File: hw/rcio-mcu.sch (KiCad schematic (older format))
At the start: 26 parts

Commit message: hw: Use PB9 (TIM17 CH1) for FAN RPM input
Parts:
- removed XP?: FAN, symbol Connector_Generic:Conn_01x02
- added XP?: FAN, symbol Connector_Generic:Conn_01x03
- R?: value 10k -> 4.7k
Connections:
- net labels added: FAN_RPM
- no-connect marks 15 -> 14
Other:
- moved on the sheet: DD?, R?, XP?

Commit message: hw: replace STM console and SWD with one connector. Rpi I2C and UART to DroneCode GPS port
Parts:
- removed XP?: SWD, symbol dronecode-conn:stm_swdo
- removed XP?: DBG UART, symbol Connector_Generic:Conn_01x03
- added R?: 47k, symbol Device:R
- added XP?: DC-Debug, symbol dronecode-conn:DC-Debug
- R?: value 4.7k -> 10k
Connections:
- net labels removed: BOOT0, ~NRST
- no-connect marks 14 -> 13
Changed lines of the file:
@@
 $EndDescr
-$Comp
-L dronecode-conn:stm_swdo XP?
-U 1 1 5AC130B8
-P 13250 8100
-F 0 "XP?" H 13478 8153 60  0000 L CNN
-F 1 "SWD" H 13478 8047 60  0000 L CNN
-F 2 "" H 13250 8100 60  0001 C CNN
-F 3 "" H 13250 8100 60  0001 C CNN
-	1    13250 8100
-	1    0    0    -1
-$EndComp
 $Comp
 L MCU_ST_STM32:STM32F030CCTx DD?
@@
 Wire Wire Line
 	3750 2050 4800 2050
-Text Label 4000 2050 0    60   ~ 0
-~NRST
 $Comp
 L power:+3.3V #PWR?
 U 1 1 5AC3643C
-P 12700 7700
-F 0 "#PWR?" H 12700 7550 50  0001 C CNN
-F 1 "+3.3V" H 12715 7873 50  0000 C CNN
-F 2 "" H 12700 7700 50  0001 C CNN
-F 3 "" H 12700 7700 50  0001 C CNN
-	1    12700 7700
+P 11900 7950
+F 0 "#PWR?" H 11900 7800 50  0001 C CNN
+F 1 "+3.3V" H 11915 8123 50  0000 C CNN
+F 2 "" H 11900 7950 50  0001 C CNN
+F 3 "" H 11900 7950 50  0001 C CNN
+	1    11900 7950
 	1    0    0    -1
 $EndComp
@@
 $EndComp
 Wire Wire Line
-	12850 7850 12700 7850
-Wire Wire Line
-	12700 7850 12700 7700
-Wire Wire Line
-	12850 8050 12700 8050
-Wire Wire Line
-	12700 8050 12700 8500
-Wire Wire Line
-	12850 7950 12300 7950
-Wire Wire Line
-	12850 8150 12300 8150
-Wire Wire Line
-	12850 8250 12300 8250
-Text Label 12300 7950 0    60   ~ 0
+	12050 8500 11500 8500
+Wire Wire Line
+	12050 8400 11500 8400
+Text Label 11500 8500 0    60   ~ 0
 SWCLK
-Text Label 12300 8150 0    60   ~ 0
+Text Label 11500 8400 0    60   ~ 0
 SWDIO
-Text Label 12300 8250 0    60   ~ 0
-~NRST
 Text GLabel 11300 3850 2    60   Input ~ 0
 RPI_SPI0_MOSI
@@
 Text GLabel 11300 4250 2    60   Output ~ 0
 SERVO3
-Text GLabel 13050 2600 0    60   UnSpc ~ 0
+Text GLabel 13050 2200 0    60   UnSpc ~ 0
 ADC_Vbat
-Text GLabel 13050 2450 0    60   UnSpc ~ 0
+Text GLabel 13850 2600 2    60   UnSpc ~ 0
 ADC_V5hat
 $Comp
@@
 Wire Wire Line
 	13600 3650 13600 3750
-Wire Wire Line
-	13050 2600 13200 2600
 $Comp
 L power:GND #PWR?
@@
 P 13200 3500
 F 0 "R?" H 13270 3546 50  0000 L CNN
-F 1 "4.7k" H 13270 3455 50  0000 L CNN
+F 1 "10k" H 13270 3455 50  0000 L CNN
 F 2 "" V 13130 3500 50  0001 C CNN
 F 3 "~" H 13200 3500 50  0001 C CNN
@@
 Wire Wire Line
 	13200 3650 13200 3750
-Wire Wire Line
-	13200 2600 13200 2750
-NoConn ~ 12850 8350
 $Comp
 L power:GND #PWR?
 U 1 1 5AC640AE
-P 12700 8500
-F 0 "#PWR?" H 12700 8250 50  0001 C CNN
-F 1 "GND" H 12705 8327 50  0000 C CNN
-F 2 "" H 12700 8500 50  0001 C CNN
-F 3 "" H 12700 8500 50  0001 C CNN
-	1    12700 8500
+P 11900 8750
+F 0 "#PWR?" H 11900 8500 50  0001 C CNN
+F 1 "GND" H 11905 8577 50  0000 C CNN
+F 2 "" H 11900 8750 50  0001 C CNN
+F 3 "" H 11900 8750 50  0001 C CNN
+	1    11900 8750
 	1    0    0    -1
 $EndComp
@@
 Text Label 3700 4150 0    60   ~ 0
 Rx_S.port
-Text Label 3950 2250 0    60   ~ 0
-BOOT0
 $Comp
 L Device:R R?
@@
 Wire Wire Line
 	11300 3950 10600 3950
-$Comp
-L Connector_Generic:Conn_01x03 XP?
-U 1 1 5ACE5EC5
-P 12650 4150
-F 0 "XP?" H 12729 4192 50  0000 L CNN
-F 1 "DBG UART" H 12729 4101 50  0000 L CNN
-F 2 "" H 12650 4150 50  0001 C CNN
-F 3 "~" H 12650 4150 50  0001 C CNN
-	1    12650 4150
-	1    0    0    -1
-$EndComp
-Wire Wire Line
-	10600 4050 12450 4050
-Wire Wire Line
-	12450 4150 10600 4150
-$Comp
-L power:GND #PWR?
-U 1 1 5ACEF9E6
-P 12350 4350
-F 0 "#PWR?" H 12350 4100 50  0001 C CNN
-F 1 "GND" H 12355 4177 50  0000 C CNN
-F 2 "" H 12350 4350 50  0001 C CNN
-F 3 "" H 12350 4350 50  0001 C CNN
-	1    12350 4350
-	1    0    0    -1
-$EndComp
-Wire Wire Line
-	12450 4250 12350 4250
-Wire Wire Line
-	12350 4250 12350 4350
-Text Label 11800 4050 0    60   ~ 0
+Wire Wire Line
+	10600 4050 11300 4050
+Wire Wire Line
+	11300 4150 10600 4150
+Text Label 11300 4050 2    60   ~ 0
 STM_U1_TX
-Text Label 11800 4150 0    60   ~ 0
+Text Label 11300 4150 2    60   ~ 0
 STM_U1_RX
 Wire Wire Line
@@
 	13600 3250 13600 3350
 Wire Wire Line
-	13050 2450 13600 2450
-Wire Wire Line
-	13600 2450 13600 2750
+	13600 2600 13600 2750
 Wire Wire Line
 	2700 2450 2700 2250
@@
 Wire Wire Line
 	2700 2250 4800 2250
+Wire Wire Line
+	13600 2600 13850 2600
+$Comp
+L Device:R R?
+U 1 1 5AD96419
+P 13200 2500
+F 0 "R?" H 13270 2546 50  0000 L CNN
+F 1 "47k" H 13270 2455 50  0000 L CNN
+F 2 "" V 13130 2500 50  0001 C CNN
+F 3 "~" H 13200 2500 50  0001 C CNN
+	1    13200 2500
+	1    0    0    -1
+$EndComp
+Wire Wire Line
+	13050 2200 13200 2200
+Wire Wire Line
+	13200 2200 13200 2350
+Wire Wire Line
+	13200 2650 13200 2750
+$Comp
+L dronecode-conn:DC-Debug XP?
+U 1 1 5ADD0906
+P 12450 8350
+F 0 "XP?" H 12678 8403 60  0000 L CNN
+F 1 "DC-Debug" H 12678 8297 60  0000 L CNN
+F 2 "" H 12400 8350 60  0001 C CNN
+F 3 "" H 12400 8350 60  0001 C CNN
+	1    12450 8350
+	1    0    0    -1
+$EndComp
+Wire Wire Line
+	12050 8300 11500 8300
+Wire Wire Line
+	12050 8200 11500 8200
+Text Label 11500 8200 0    60   ~ 0
+STM_U1_TX
+Text Label 11500 8300 0    60   ~ 0
+STM_U1_RX
+Wire Wire Line
+	12050 8100 11900 8100
+Wire Wire Line
+	11900 8100 11900 7950
+Wire Wire Line
+	12050 8600 11900 8600
+Wire Wire Line
+	11900 8600 11900 8750
 $EndSCHEMATC

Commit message: hw: sch ready
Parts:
- gave numbers to parts that had none: 26

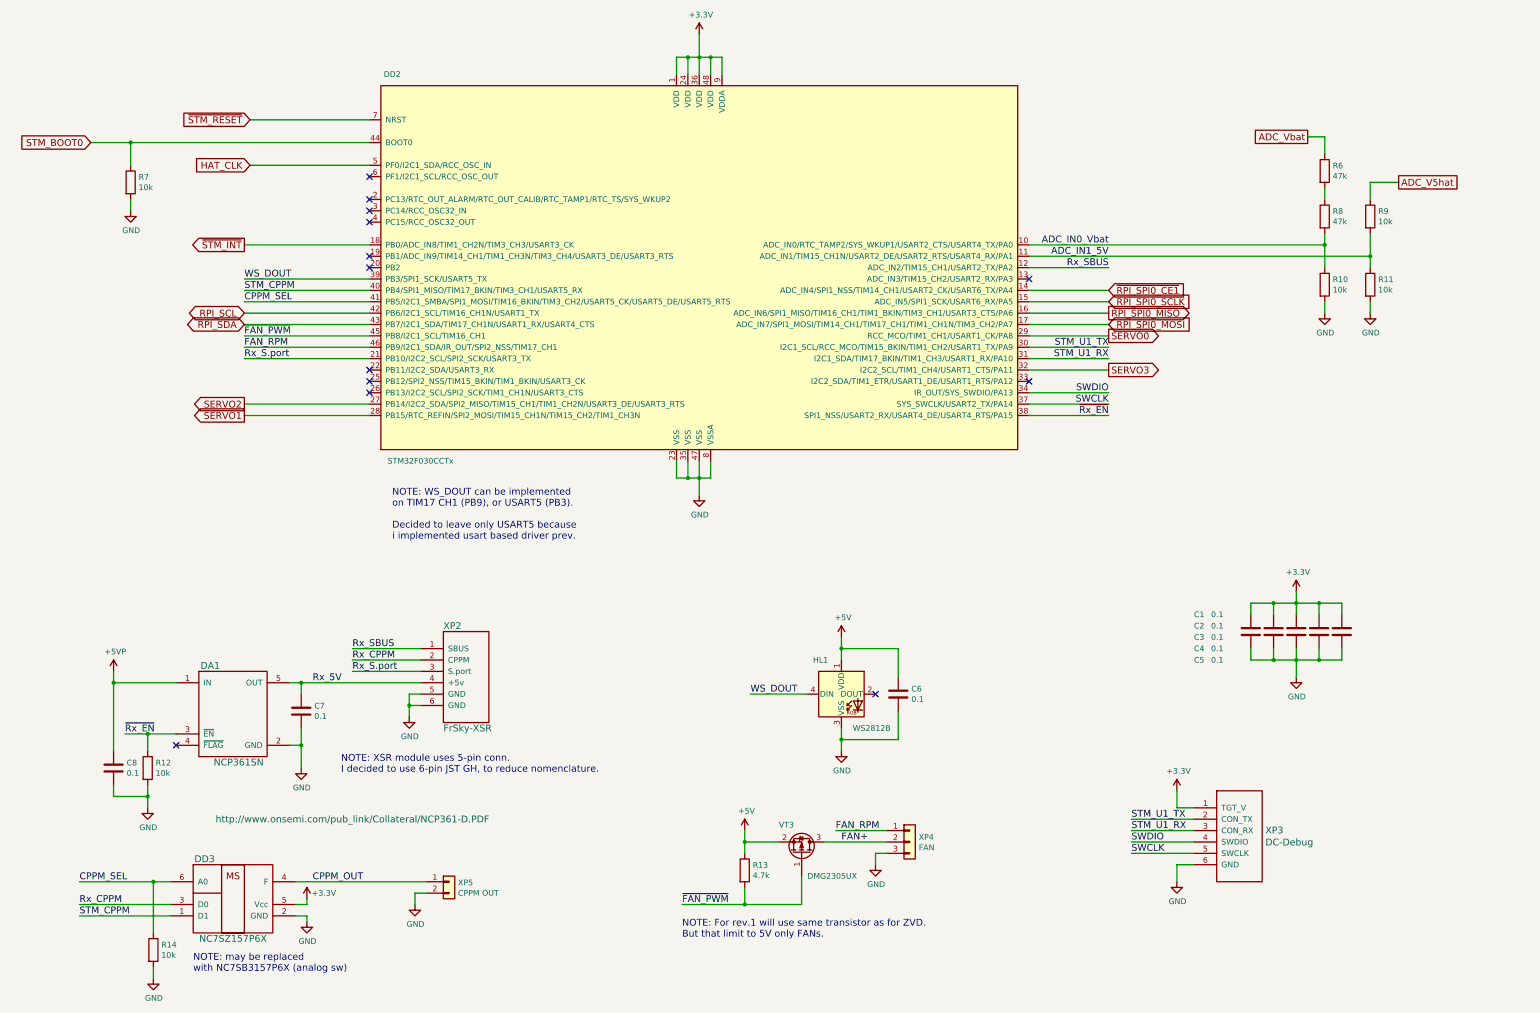
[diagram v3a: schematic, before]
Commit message: hw: cvpcb for R,C
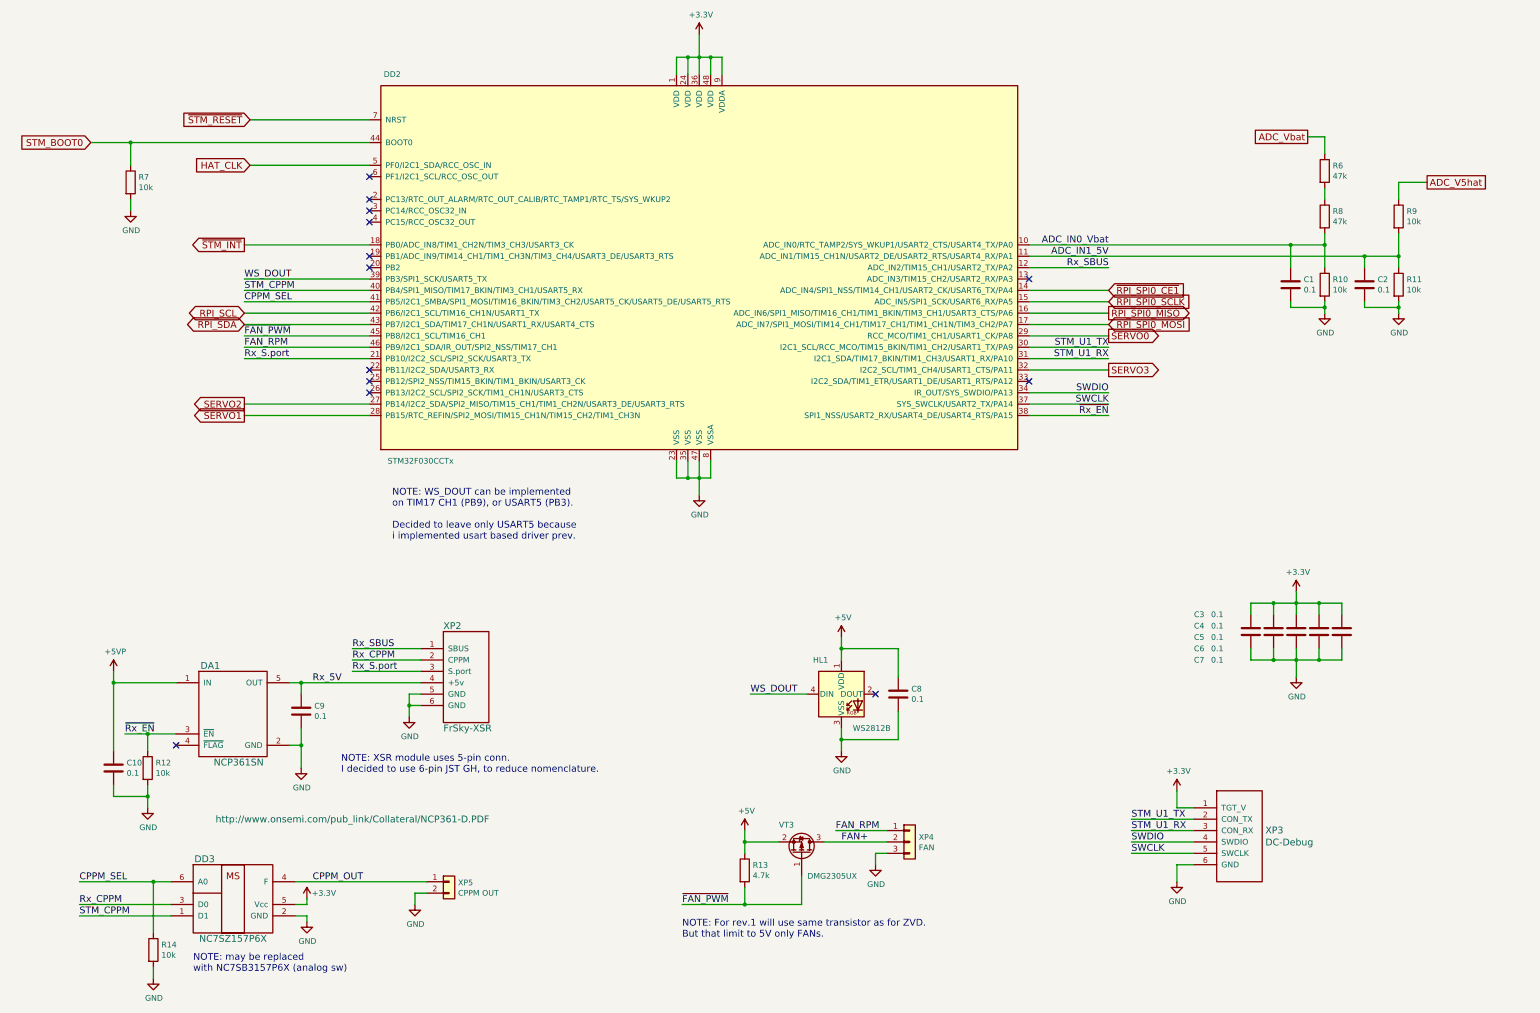
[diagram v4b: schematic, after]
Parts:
- added C1, C2: 0.1, Capacitor_SMD:C_0603_1608Metric, symbol Device:C
- C10: renamed from C8; footprint (none) -> Capacitor_SMD:C_0603_1608Metric
- C3: renamed from C1; footprint (none) -> Capacitor_SMD:C_0603_1608Metric
- C4: renamed from C2; footprint (none) -> Capacitor_SMD:C_0603_1608Metric
- C5: renamed from C3; footprint (none) -> Capacitor_SMD:C_0603_1608Metric
- C6: renamed from C4; footprint (none) -> Capacitor_SMD:C_0603_1608Metric
- C7: renamed from C5; footprint (none) -> Capacitor_SMD:C_0603_1608Metric
- C8: renamed from C6; footprint (none) -> Capacitor_SMD:C_0603_1608Metric
- C9: renamed from C7; footprint (none) -> Capacitor_SMD:C_0603_1608Metric
- DA1: footprint (none) -> Package_TO_SOT_SMD:SOT-23-5_HandSoldering
- R10, R11, R12, R13, R14, R6, R7, R8, R9: footprint (none) -> Resistor_SMD:R_0603_1608Metric
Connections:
- net ADC_IN0_Vbat: now also C1.1
- net ADC_IN1_5V: now also C2.1
- net GND: now also C1.2, C2.2
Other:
- moved on the sheet: R11, R9

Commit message: hw: more cvpcb
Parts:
- XP2: footprint (none) -> Connector_JST:JST_GH_SM06B-GHS-TB_1x06-1MP_P1.25mm_Horizontal
- XP3: footprint (none) -> Connector_JST:JST_GH_BM06B-GHS-TBT_1x06-1MP_P1.25mm_Vertical
- XP4: footprint (none) -> Connector:FanPinHeader_1x03_P2.54mm_Vertical
- XP5: footprint (none) -> Connector_JST:JST_PH_B2B-PH-K_1x02_P2.00mm_Vertical
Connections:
- net FAN_RPM: now also XP4.3 (Pin_3); no longer XP4.1 (Pin_1)
- net GND: now also XP4.1 (Pin_1); no longer XP4.3 (Pin_3)
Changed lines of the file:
@@
 F 0 "XP2" H 5450 7400 60  0000 L CNN
 F 1 "FrSky-XSR" H 5450 6500 60  0000 L CNN
-F 2 "" H 5650 6950 60  0001 C CNN
+F 2 "Connector_JST:JST_GH_SM06B-GHS-TB_1x06-1MP_P1.25mm_Horizontal" H 5650 6950 60  0001 C CNN
 F 3 "" H 5650 6950 60  0001 C CNN
 	1    5650 6950
@@
 F 0 "XP5" H 5579 8742 50  0000 L CNN
 F 1 "CPPM OUT" H 5579 8651 50  0000 L CNN
-F 2 "" H 5500 8750 50  0001 C CNN
+F 2 "Connector_JST:JST_PH_B2B-PH-K_1x02_P2.00mm_Vertical" H 5500 8750 50  0001 C CNN
 F 3 "~" H 5500 8750 50  0001 C CNN
 	1    5500 8750
@@
 F 0 "XP4" H 9630 8442 50  0000 L CNN
 F 1 "FAN" H 9630 8351 50  0000 L CNN
-F 2 "" H 9550 8400 50  0001 C CNN
+F 2 "Connector:FanPinHeader_1x03_P2.54mm_Vertical" H 9550 8400 50  0001 C CNN
 F 3 "~" H 9550 8400 50  0001 C CNN
 	1    9550 8400
-	1    0    0    -1
+	1    0    0    1
 $EndComp
 Wire Wire Line
@@
 F 0 "XP3" H 12678 8403 60  0000 L CNN
 F 1 "DC-Debug" H 12678 8297 60  0000 L CNN
-F 2 "" H 12400 8350 60  0001 C CNN
+F 2 "Connector_JST:JST_GH_BM06B-GHS-TBT_1x06-1MP_P1.25mm_Vertical" H 12400 8350 60  0001 C CNN
 F 3 "" H 12400 8350 60  0001 C CNN
 	1    12450 8350

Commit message: hw: only custom packages left unassigned
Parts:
- DD3: footprint (none) -> Package_TO_SOT_SMD:SOT-363_SC-70-6_Handsoldering
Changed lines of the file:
@@
 F 0 "DD3" H 3350 9350 60  0000 C CNN
 F 1 "NC7SZ157P6X" H 3600 8650 60  0000 C CNN
-F 2 "" H 3600 8950 60  0001 C CNN
+F 2 "Package_TO_SOT_SMD:SOT-363_SC-70-6_Handsoldering" H 3600 8950 60  0001 C CNN
 F 3 "https://www.terraelectronica.ru/pdf/show?pdf_file=%252Fds%252Fpdf%252FN%252Fnc7sz157p6x.pdf" H 3600 8950 60  0001 C CNN
 	1    3600 8950

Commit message: hw: wonring on NET
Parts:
- VT3: footprint TO_SOT_Packages_SMD:SOT-23_Handsoldering -> Package_TO_SOT_SMD:SOT-23_Handsoldering
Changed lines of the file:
@@
 F 0 "VT3" V 8850 8300 50  0000 L CNN
 F 1 "DMG2305UX" V 8400 8550 50  0000 L CNN
-F 2 "TO_SOT_Packages_SMD:SOT-23_Handsoldering" H 8800 8600 50  0001 C CNN
+F 2 "Package_TO_SOT_SMD:SOT-23_Handsoldering" H 8800 8600 50  0001 C CNN
 F 3 "" H 8600 8500 50  0001 C CNN
 	1    8600 8500

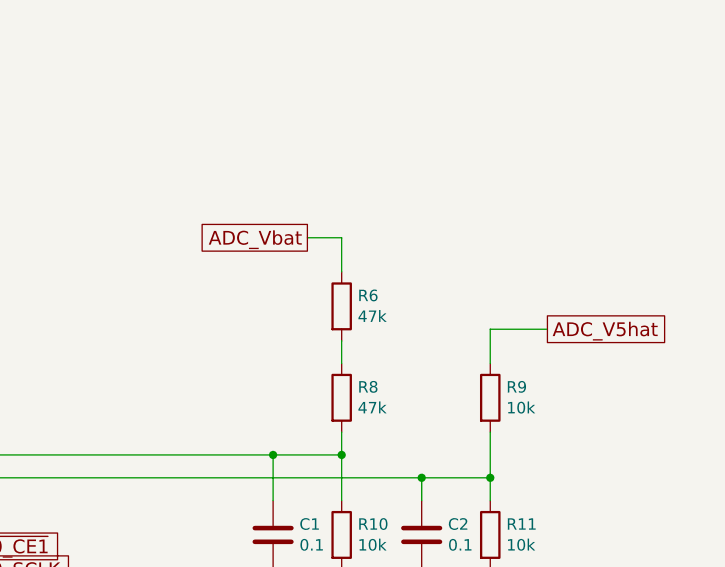
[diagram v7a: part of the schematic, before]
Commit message: hw: add battery input connector
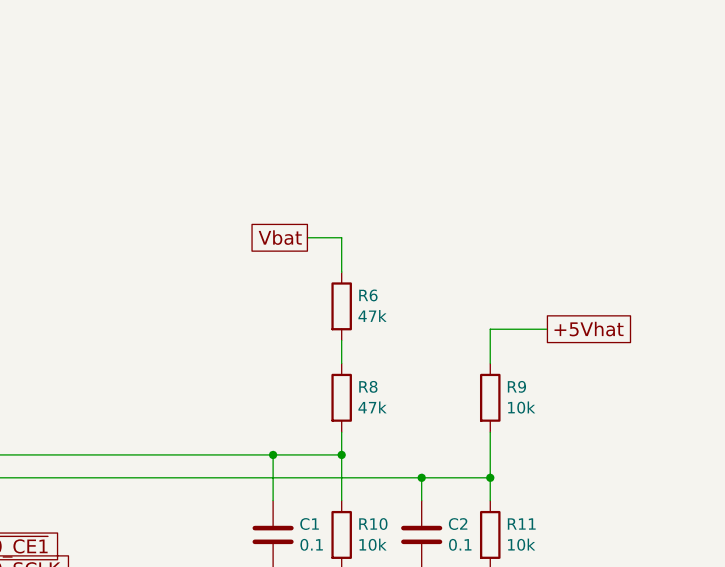
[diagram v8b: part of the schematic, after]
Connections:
- net ADC_V5hat renamed +5Vhat
- net ADC_Vbat renamed Vbat
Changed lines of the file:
@@
 SERVO3
 Text GLabel 13050 2200 0    60   UnSpc ~ 0
-ADC_Vbat
+Vbat
 Text GLabel 14100 2600 2    60   UnSpc ~ 0
-ADC_V5hat
++5Vhat
 $Comp
 L dronecode-conn:FrSky-XSR XP2
